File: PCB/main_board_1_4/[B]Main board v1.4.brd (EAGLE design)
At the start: 123 x 70 mm, 117 parts, among them J1 6P_CONN, J2 RJ11MX-95001-2661, J3 POWER_JACKPTH, J4 RJ45_MX-95001-2881, J5 RJ45_MX-95001-2881, J6 RJ45_MX-95001-2881, J7 10104111-0001LF, K1 RELAY, K2 RELAY, Q1 BC807-40SMD, T3 IRLML2244, T4 2N7002PW, U4 VREG_MIC5216, U5 TPS62133RGTT, U6 CC2D23-CHIPCAP2, U7 PIC24FJ256GB206, U8 LMC555

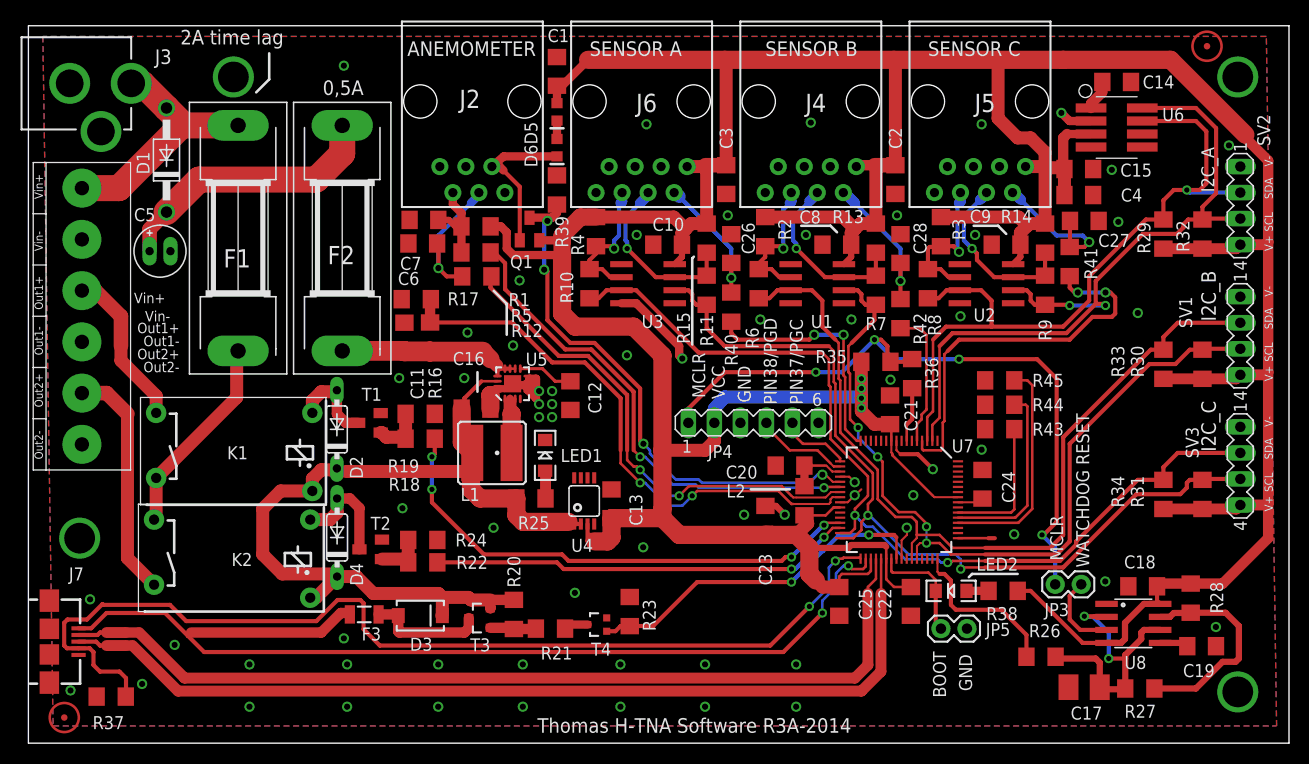
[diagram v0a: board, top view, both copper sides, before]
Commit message: Latest revision of PCB with support for RainGauge and some other sensors.
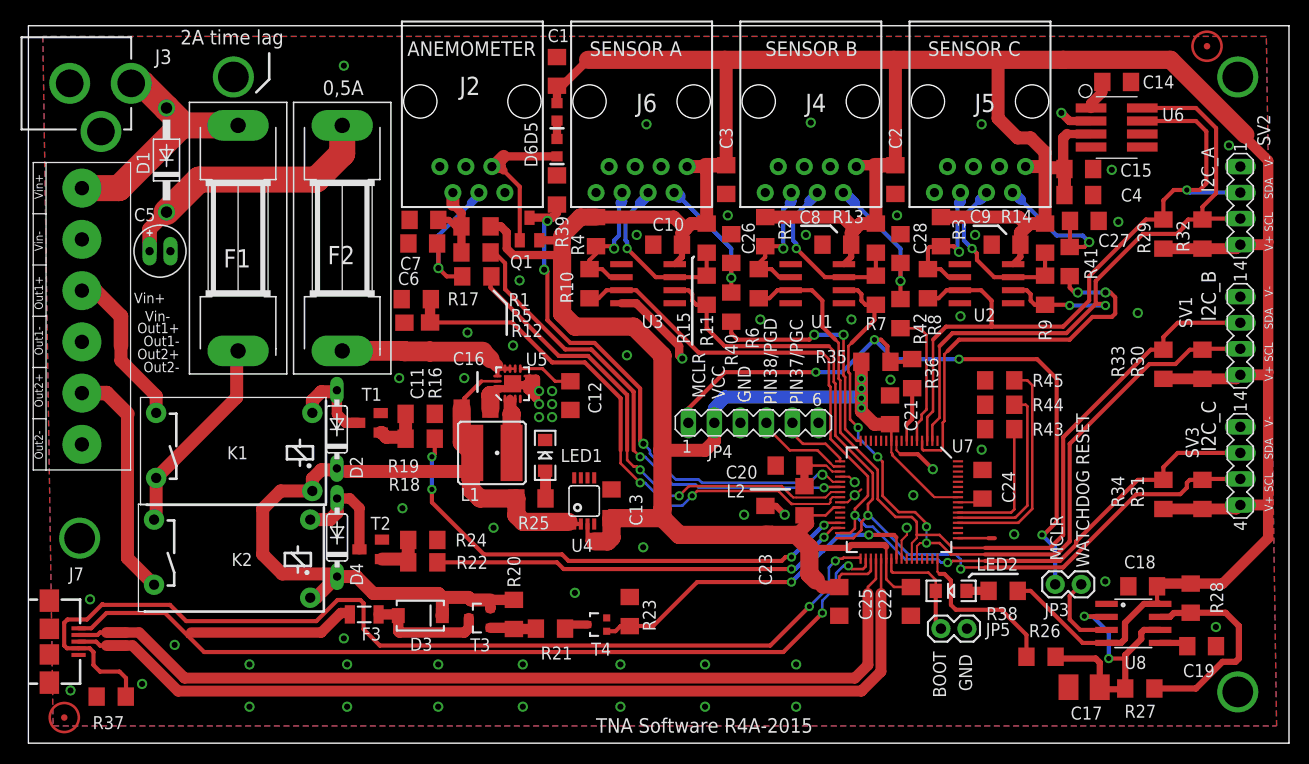
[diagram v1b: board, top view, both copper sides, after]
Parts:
- J2: value RJ11MX-95001-2661 -> RJ12MX-95001-2661
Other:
- board text added: "TNA Software R4A-2015"
- board text removed: "Thomas H-TNA Software R2A-2013"
- board text removed: "Thomas H-TNA Software R3A-2014"
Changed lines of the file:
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@@
 <text x="24.905" y="69.595" size="1.4224" layer="25" rot="R180">2A time lag</text>
 <text x="28.715" y="63.245" size="1.4224" layer="25">0,5A </text>
-<text x="49.67" y="1.015" size="1.4224" layer="25" font="vector">Thomas H-TNA Software R3A-2014 </text>
-<text x="87.135" y="1.015" size="1.4224" layer="26" font="vector" rot="MR0">Thomas H-TNA Software R2A-2013</text>
+<text x="55.385" y="1.015" size="1.4224" layer="25" font="vector">TNA Software R4A-2015</text>
+<text x="81.42" y="1.015" size="1.4224" layer="26" font="vector" rot="MR0">TNA Software R4A-2015</text>
 <text x="36.97" y="67.055" size="1.4224" layer="25" font="vector">ANEMOMETER</text>
 <text x="54.75" y="67.055" size="1.4224" layer="25" font="vector">SENSOR A</text>
@@
 <attribute name="VALUE" x="15.38" y="45.846" size="1.27" layer="27" ratio="10"/>
 </element>
-<element name="J2" library="Thomas Egnal Library" package="MX-95001-2661" value="RJ11MX-95001-2661" x="43.32" y="62.61" smashed="yes" rot="R180">
-<attribute name="NAME" x="42.05" y="61.975" size="1.778" layer="25"/>
-<attribute name="VALUE" x="49.035" y="60.07" size="1.778" layer="27" rot="R180"/>
-<attribute name="VENDOR" value="TME" x="43.32" y="62.61" size="1.778" layer="27" rot="R180" display="off"/>
-<attribute name="LINK" value="http://www.tme.eu/pl/katalog/?idp=1&amp;search=mx-95001-2661&amp;cleanParameters=1" x="43.32" y="62.61" size="1.778" layer="27" rot="R180" display="off"/>
-</element>
 <element name="C14" library="rcl" package="C1206" value="100n" x="106.185" y="64.515" smashed="yes">
 <attribute name="NAME" x="108.725" y="63.88" size="1.27" layer="25"/>
@@
 <attribute name="NAME" x="97.94875" y="34.76625" size="1.27" layer="25"/>
 <attribute name="VALUE" x="93.50375" y="32.86125" size="1.27" layer="27"/>
+</element>
+<element name="J2" library="Thomas Egnal Library" package="MX-95001-2661" value="RJ12MX-95001-2661" x="43.32" y="62.61" smashed="yes" rot="R180">
+<attribute name="VENDOR" value="TME" x="43.32" y="62.61" size="1.778" layer="27" rot="R180" display="off"/>
+<attribute name="LINK" value="http://www.tme.eu/pl/katalog/?idp=1&amp;search=mx-95001-2661&amp;cleanParameters=1" x="43.32" y="62.61" size="1.778" layer="27" rot="R180" display="off"/>
+<attribute name="NAME" x="42.05" y="63.245" size="1.778" layer="25"/>
+<attribute name="VALUE" x="49.035" y="60.07" size="1.778" layer="27" rot="R180"/>
 </element>
 </elements>
@@
 <contactref element="R17" pad="2"/>
 <contactref element="C5" pad="-"/>
-<contactref element="J2" pad="4"/>
 <contactref element="C14" pad="2"/>
 <contactref element="C15" pad="1"/>
@@
 <via x="90.945" y="41.655" extent="1-16" drill="0.6" diameter="0.8128"/>
 <via x="36.49375" y="22.9225" extent="1-16" drill="0.6" diameter="0.8128"/>
+<contactref element="J2" pad="4"/>
 </signal>
 <signal name="+5V" class="1">
@@
 <contactref element="R12" pad="2"/>
 <contactref element="C6" pad="2"/>
-<contactref element="J2" pad="5"/>
-<wire x1="41.415" y1="53.72" x2="41.415" y2="52.565" width="0.8128" layer="1"/>
 <wire x1="41.415" y1="52.565" x2="42.253" y2="51.727" width="0.8128" layer="1"/>
 <wire x1="42.253" y1="50.42" x2="42.253" y2="51.727" width="0.8128" layer="1"/>
@@
 <wire x1="42.253" y1="50.42" x2="41.655" y2="50.42" width="0.6096" layer="1"/>
 <wire x1="41.655" y1="50.42" x2="41.02" y2="51.055" width="0.6096" layer="1"/>
+<contactref element="J2" pad="5"/>
+<wire x1="41.415" y1="53.72" x2="41.415" y2="52.565" width="1.27" layer="1"/>
 </signal>
 <signal name="N$4">
 <contactref element="R5" pad="2"/>
 <contactref element="C7" pad="2"/>
-<contactref element="J2" pad="3"/>
-<wire x1="43.955" y1="53.72" x2="43.955" y2="53.48" width="0.8128" layer="16"/>
 <wire x1="43.955" y1="53.48" x2="43.18" y2="52.705" width="0.8128" layer="16"/>
 <wire x1="43.18" y1="52.705" x2="40.005" y2="49.53" width="0.4064" layer="16"/>
@@
 <wire x1="42.3305" y1="45.5425" x2="40.8175" y2="45.5425" width="0.4064" layer="1"/>
 <wire x1="40.8175" y1="45.5425" x2="40.005" y2="46.355" width="0.4064" layer="1"/>
+<contactref element="J2" pad="3"/>
+<wire x1="43.955" y1="53.48" x2="43.955" y2="53.72" width="1.27" layer="16"/>
 </signal>
 <signal name="TEMP1/SCL1">
@@
 </signal>
 <signal name="N$15">
-<contactref element="J2" pad="2"/>
 <contactref element="D6" pad="C"/>
 <contactref element="Q1" pad="B"/>
@@
 <wire x1="47.945" y1="54.29" x2="46.355" y2="55.88" width="0.4064" layer="1"/>
 <wire x1="51.575" y1="57.2525" x2="46.37625" y2="57.2525" width="0.8128" layer="1"/>
-<wire x1="46.37625" y1="57.2525" x2="45.225" y2="56.26" width="0.8128" layer="1"/>
-<wire x1="45.225" y1="56.26" x2="45.975" y2="56.26" width="0.8128" layer="1"/>
 <wire x1="45.975" y1="56.26" x2="46.355" y2="55.88" width="0.8128" layer="1"/>
+<contactref element="J2" pad="2"/>
+<wire x1="45.225" y1="56.26" x2="45.38375" y2="56.26" width="1.27" layer="1"/>
+<wire x1="45.38375" y1="56.26" x2="46.37625" y2="57.2525" width="1.27" layer="1"/>
+<wire x1="45.38375" y1="56.26" x2="45.975" y2="56.26" width="1.27" layer="1"/>
 </signal>
 <signal name="N$18">
